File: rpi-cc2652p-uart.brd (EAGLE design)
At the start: 46.2 x 20.5 mm, 13 parts, among them U1 CC2652P2-DUOWEISI, U2 AP2112K

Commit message: lib updates
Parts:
- U1: device codm:CC2653P2-DUOWEISI -> codm:CC2652P2-DUOWEISI
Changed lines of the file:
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@@
 </layers>
 <board>
-<fusionsync huburn="a.cGVyc29uYWw6dWUyYzE1ODk4" projecturn="a.cGVyc29uYWw6dWUyYzE1ODk4IzIwMTkwNTIyMTk1MjcwNTc2" f3durn="urn:adsk.wipprod:dm.lineage:nieUfFR7S1OBw6zG4Cdbvg" pcbguid="b1ec303d-6b34-49b1-8bfc-5f58fc53c131" lastpulledtime="" lastsyncedchangeguid="" latestrevisionid="3180c41f-1742-4242-9b77-597a26722937" lastsyncedrevisionid="3180c41f-1742-4242-9b77-597a26722937" lastboardhashguid="7fd4f6dc-4d28-9e05-959b-787379fa6ace" lastpushedtime="2021-11-22T12:30:24Z" linktopcb3d="true"/>
+<fusionsync huburn="a.cGVyc29uYWw6dWUyYzE1ODk4" projecturn="a.cGVyc29uYWw6dWUyYzE1ODk4IzIwMTkwNTIyMTk1MjcwNTc2" f3durn="urn:adsk.wipprod:dm.lineage:nieUfFR7S1OBw6zG4Cdbvg" pcbguid="" lastpulledtime="" lastsyncedchangeguid="" latestrevisionid="0bb0c984-b6d6-40b6-8696-d23dd2e1ef8c" lastsyncedrevisionid="0bb0c984-b6d6-40b6-8696-d23dd2e1ef8c" lastboardhashguid="1cd7a30e-5d0a-9469-b4f9-0f2efae1d7c0" lastpushedtime="2022-03-01T09:58:48Z" linktopcb3d="true"/>
 <plain>
 <wire x1="7.6" y1="0" x2="43.6" y2="0" width="0" layer="20"/>
@@
 <attribute name="VALUE" x="7.41" y="-0.27" size="0.8128" layer="27"/>
 </element>
-<element name="U1" library="codm" library_urn="urn:adsk.eagle:library:11602856" package="CC2653P2-DUOWEISI" package3d_urn="urn:adsk.eagle:package:27394862/4" value="CC2652P2-DUOWEISI" x="15.8" y="18.5" smashed="yes" rot="R270"/>
+<element name="U1" library="codm" library_urn="urn:adsk.eagle:library:11602856" package="CC2652P2-DUOWEISI" package3d_urn="urn:adsk.eagle:package:27394862/7" value="CC2652P2-DUOWEISI" x="15.8" y="18.5" smashed="yes" rot="R270"/>
 <element name="C2" library="rcl" library_urn="urn:adsk.eagle:library:334" package="C0805" package3d_urn="urn:adsk.eagle:package:23617/2" value="1u" x="7.8" y="6.7" smashed="yes" rot="R270">
 <attribute name="NAME" x="6.7916" y="6.7" size="0.8128" layer="25" align="center-right"/>

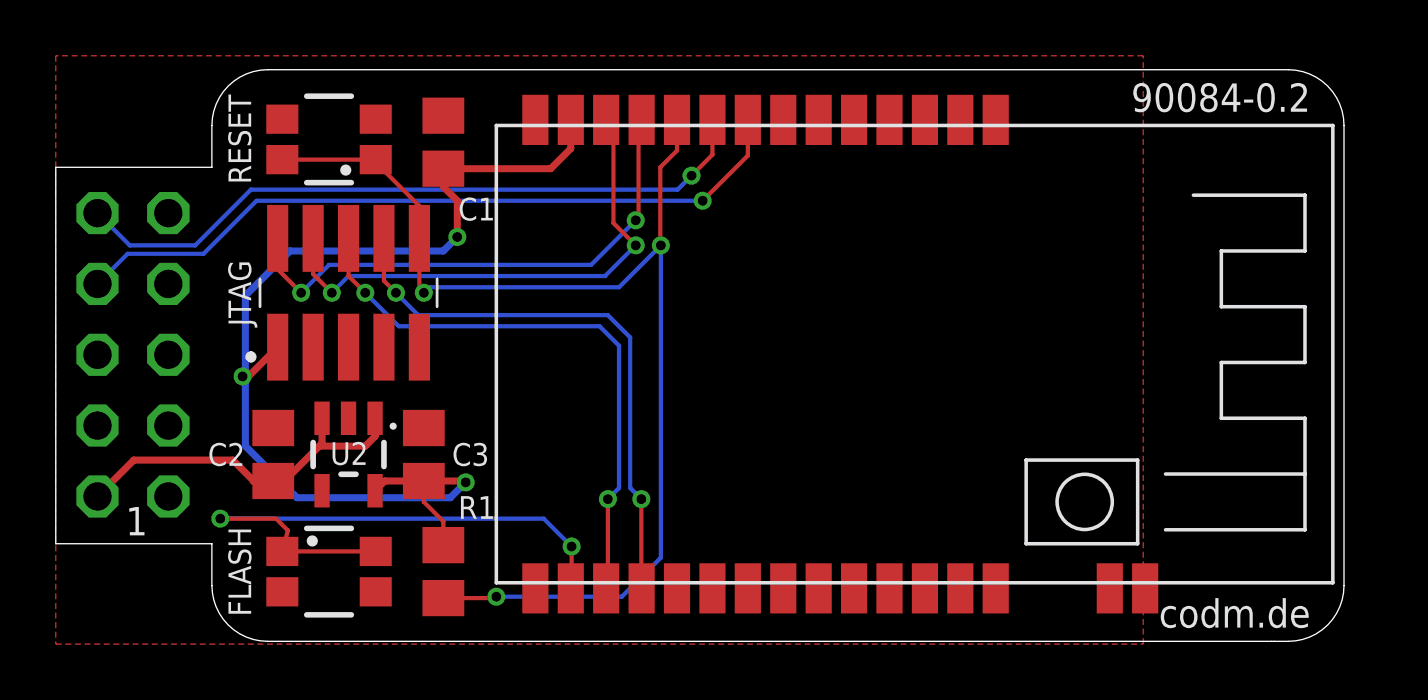
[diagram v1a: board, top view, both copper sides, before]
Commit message: 0805 to 0603
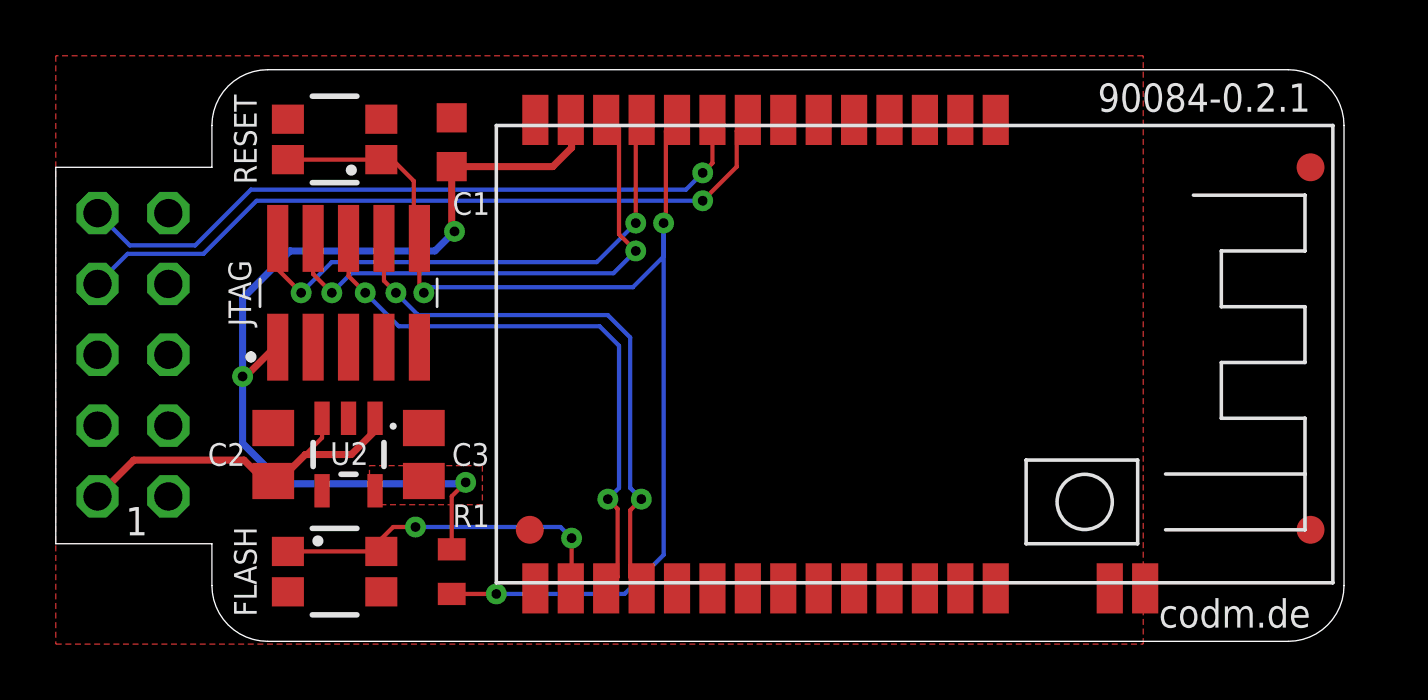
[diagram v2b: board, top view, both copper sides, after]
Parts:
- added FD1, FD2, FD3: FIDUCIAL1X2, SparkFun-Aesthetics:FIDUCIAL-1X2
- C1: device rcl:C0805 -> rcl:C0603K
- R1: device rcl:R0805 -> codm:R0603RF
- moved U$4 6.40 mm to (30.3, 5.50)
- moved U$3 3.90 mm to (24.0, 6.30)
- moved C1 0.30 mm to (14.2, 17.9)
- moved R1 0.30 mm to (14.2, 2.50)
- moved FLASH 0.20 mm to (10.0, 2.50)
- moved RESET 0.20 mm to (10.0, 18.0)
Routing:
- net FLASH: track 21.5 -> 13.0 mm
- net VCC: track 39.1 -> 34.7 mm
- net RST: track 42.4 -> 43.3 mm
- added copper zone on layer 1, net VCC
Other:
- outline, holes or cut-outs redrawn
- board text added: "90084-0.2.1"
- board text added: "90084-0.2.1 CC-BY-SA-NC"
- board text added: "CC2652P2 RPi Serial ZigBee Module V0.2.1 codm.de, (c) 2024"
- board text removed: "90084-0.2"
- board text removed: "90084-0.2 CC-BY-SA-NC"
- board text removed: "CC2652P2 RPi Serial ZigBee Module V0.2 codm.de, (c) 2021"

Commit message: added CC LED on DIO7
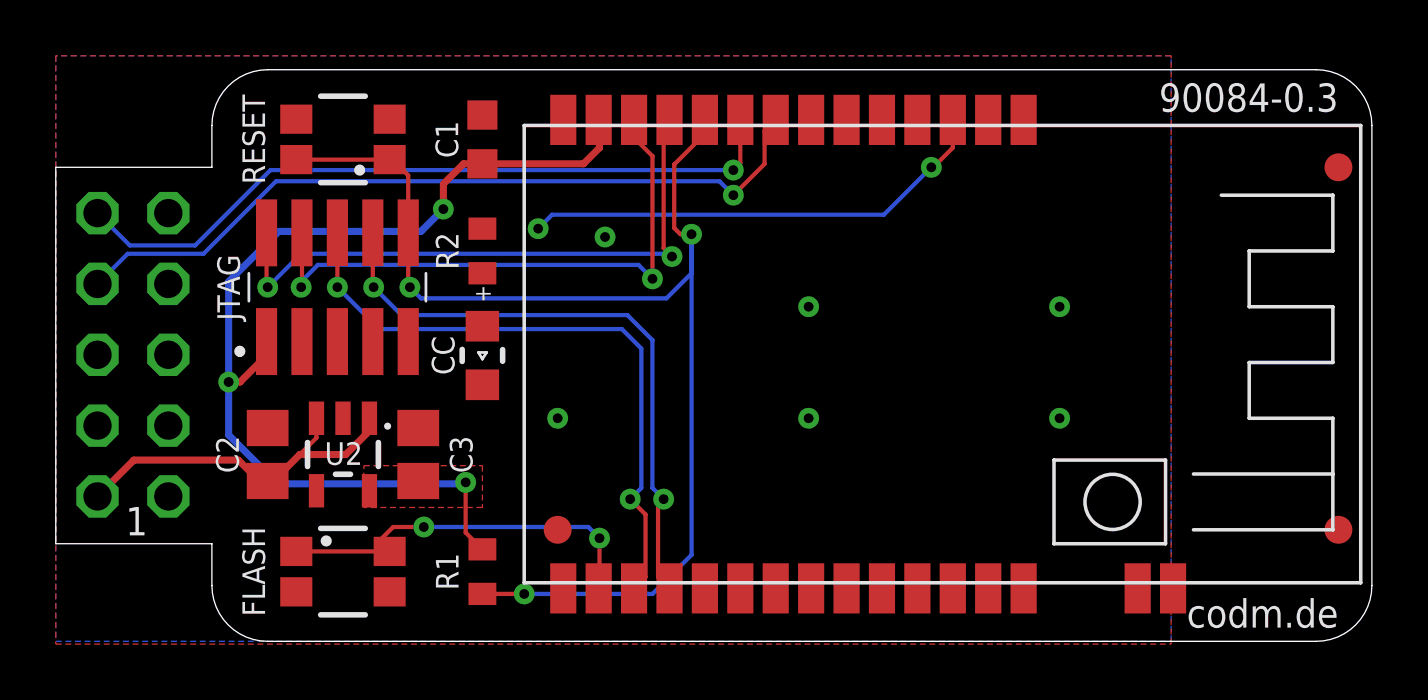
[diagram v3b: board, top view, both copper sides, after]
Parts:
- added CC: 150080YS75000, Wurth_LEDs_WL-SMCW:WL-SMCW_0805
- added R2: 1k, codm:R0603RF
- moved U$3 1.93 mm to (25.8, 5.60)
- moved C1 1.10 mm to (15.3, 18.0)
- moved R1 1.10 mm to (15.3, 2.50)
- moved FD1 1.00 mm to (46.0, 17.0)
- moved FD2 1.00 mm to (46.0, 4.00)
- moved FD3 1.00 mm to (18.0, 4.00)
- moved U$2 1.00 mm to (46.3, 16.5)
- moved U$4 1.00 mm to (31.3, 5.50)
- moved U1 1.00 mm to (16.8, 18.5)
- moved JTAG 0.45 mm to (10.1, 12.7)
- moved FLASH 0.30 mm to (10.3, 2.50)
- moved RESET 0.30 mm to (10.3, 18.0)
- moved C2 0.20 mm to (7.60, 6.70)
- moved C3 0.20 mm to (13.0, 6.70)
- moved U2 0.20 mm to (10.3, 6.70)
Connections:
- new net CC-LED: R2.1, U1.DIO7
- new net N$5: CC.2, R2.2
- net GND: now also CC.1
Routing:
- net CC-LED: track 0.00 -> 17.1 mm, vias 0 -> 2
- net TMS: track 19.1 -> 22.1 mm
- net TCK: track 19.0 -> 21.2 mm
- net VCC: track 34.7 -> 36.5 mm
- net TDO: track 21.3 -> 22.9 mm
- net RST: track 43.3 -> 44.9 mm
- net TDI: track 20.7 -> 22.1 mm
- net RXD: track 26.5 -> 27.9 mm
- net FLASH: track 13.0 -> 14.1 mm
- net TXD: track 25.3 -> 26.3 mm
- added copper zone on layer 16, net GND
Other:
- board size 46.2 x 20.5 mm -> 47.2 x 20.5 mm
- board text added: "90084-0.3"
- board text added: "90084-0.3 CC-BY-SA-NC"
- board text added: "CC2652P7 RPi Serial ZigBee Module V0.3 codm.de, (c) 2025"
- board text removed: "90084-0.2.1"
- board text removed: "90084-0.2.1 CC-BY-SA-NC"
- board text removed: "CC2652P2 RPi Serial ZigBee Module V0.2.1 codm.de, (c) 2024"
